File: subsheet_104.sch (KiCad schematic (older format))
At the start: 8 parts, among them U104 LM555_TIMER_PHY

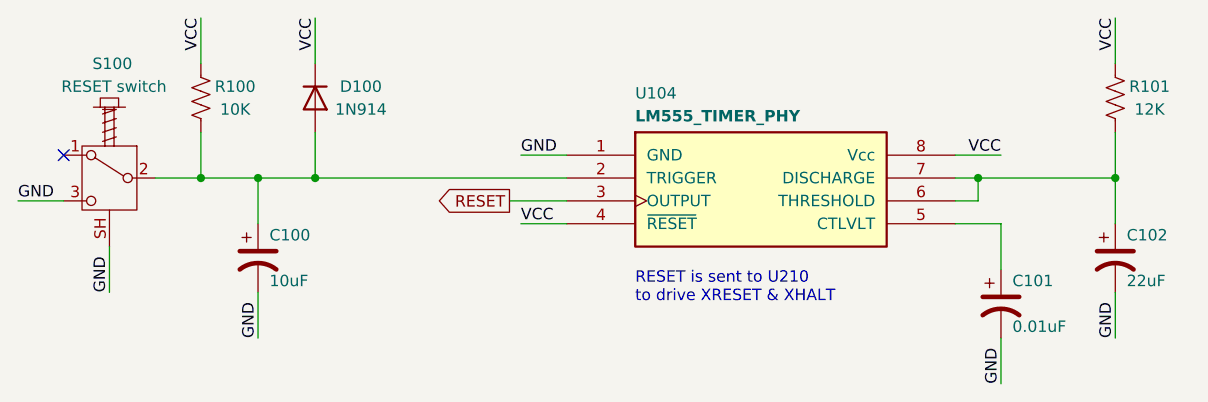
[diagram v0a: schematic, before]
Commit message: Resolves #6 : Apply the reset fix
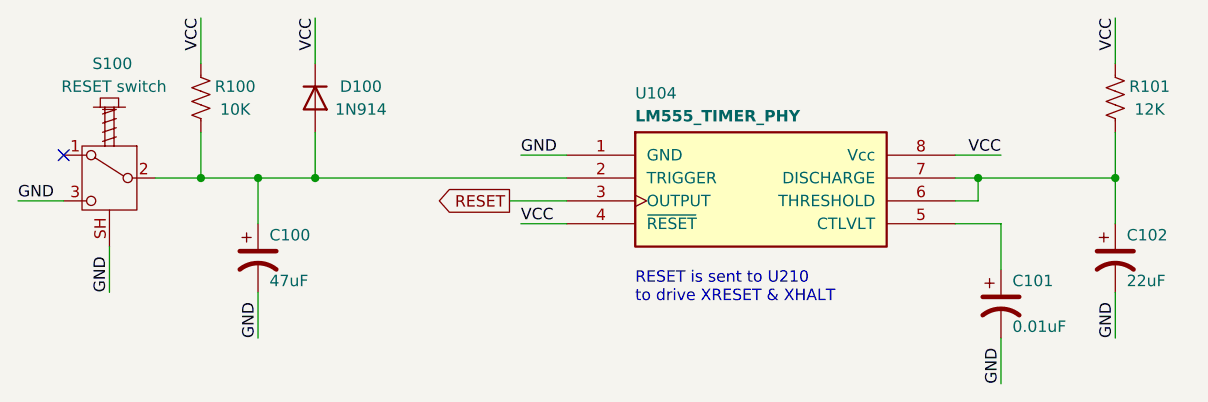
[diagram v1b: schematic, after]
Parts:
- C100: value 10uF -> 47uF
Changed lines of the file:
@@
 P 2750 2050
 F 0 "C100" H 2800 2150 50  0000 L CNN
-F 1 "10uF" H 2800 1950 50  0000 L CNN
+F 1 "47uF" H 2800 1950 50  0000 L CNN
 F 2 "commons_passives_THT:Passive_THT_capacitor_polarized_W5.08mm_L17.78mm" H 2750 2050 50  0001 C CNN
 F 3 "~" H 2750 2050 50  0001 C CNN

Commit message: Resolves #12 : Use the reference 'CP?' for polarized capacitors
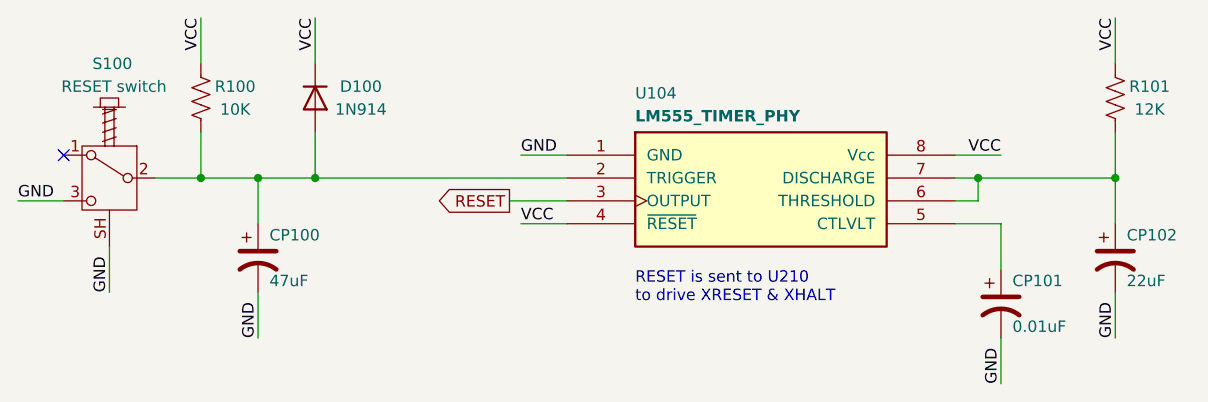
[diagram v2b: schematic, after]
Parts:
- renumbered C100 to CP100, C101 to CP101, C102 to CP102
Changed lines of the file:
@@
 VCC
 $Comp
-L Device:CP1 C100
+L Device:CP1 CP100
 U 1 1 608C1A6C
 P 2750 2050
-F 0 "C100" H 2800 2150 50  0000 L CNN
+F 0 "CP100" H 2800 2150 50  0000 L CNN
 F 1 "47uF" H 2800 1950 50  0000 L CNN
 F 2 "commons_passives_THT:Passive_THT_capacitor_polarized_W5.08mm_L17.78mm" H 2750 2050 50  0001 C CNN
@@
 	2750 2200 2750 2400
 $Comp
-L Device:CP1 C101
+L Device:CP1 CP101
 U 1 1 608C7F71
 P 6000 2250
-F 0 "C101" H 6050 2350 50  0000 L CNN
+F 0 "CP101" H 6050 2350 50  0000 L CNN
 F 1 "0.01uF" H 6050 2150 50  0000 L CNN
 F 2 "commons_passives_THT:Passive_THT_capacitor_W2.54mm_L10.16mm" H 6000 2250 50  0001 C CNN
@@
 	6000 2400 6000 2600
 $Comp
-L Device:CP1 C102
+L Device:CP1 CP102
 U 1 1 608C88D5
 P 6500 2050
-F 0 "C102" H 6550 2150 50  0000 L CNN
+F 0 "CP102" H 6550 2150 50  0000 L CNN
 F 1 "22uF" H 6550 1950 50  0000 L CNN
 F 2 "commons_passives_THT:Passive_THT_capacitor_polarized_W6.35mm_L20.32mm" H 6500 2050 50  0001 C CNN

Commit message: Resolves #13 : assign 1206 hand-solder footprints to resistors
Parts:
- R100, R101: footprint commons_passives_THT:Passive_THT_resistor_W2.54mm_L12.70mm -> Resistor_SMD:R_1206_3216Metric_Pad1.30x1.75mm_HandSolder
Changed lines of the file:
@@
 F 0 "R100" H 2650 1400 50  0000 C CNN
 F 1 "10K" H 2650 1300 50  0000 C CNN
-F 2 "commons_passives_THT:Passive_THT_resistor_W2.54mm_L12.70mm" V 2540 1340 50  0001 C CNN
+F 2 "Resistor_SMD:R_1206_3216Metric_Pad1.30x1.75mm_HandSolder" V 2540 1340 50  0001 C CNN
 F 3 "~" H 2500 1350 50  0001 C CNN
 	1    2500 1350
@@
 F 0 "R101" H 6650 1400 50  0000 C CNN
 F 1 "12K" H 6650 1300 50  0000 C CNN
-F 2 "commons_passives_THT:Passive_THT_resistor_W2.54mm_L12.70mm" V 6540 1340 50  0001 C CNN
+F 2 "Resistor_SMD:R_1206_3216Metric_Pad1.30x1.75mm_HandSolder" V 6540 1340 50  0001 C CNN
 F 3 "~" H 6500 1350 50  0001 C CNN
 	1    6500 1350

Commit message: Resolves #20 : Replace polarized capacitors CP101 and CP536 by unpolarized ones
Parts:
- C101: renamed from CP101; footprint commons_passives_THT:Passive_THT_capacitor_W2.54mm_L10.16mm -> Capacitor_SMD:C_1206_3216Metric_Pad1.33x1.80mm_HandSolder; symbol Device:CP1 -> Device:C_Small
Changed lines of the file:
@@
 	2750 2200 2750 2400
 $Comp
-L Device:CP1 CP101
+L Device:C_Small C101
 U 1 1 608C7F71
 P 6000 2250
-F 0 "CP101" H 6050 2350 50  0000 L CNN
+F 0 "C101" H 6050 2350 50  0000 L CNN
 F 1 "0.01uF" H 6050 2150 50  0000 L CNN
-F 2 "commons_passives_THT:Passive_THT_capacitor_W2.54mm_L10.16mm" H 6000 2250 50  0001 C CNN
+F 2 "Capacitor_SMD:C_1206_3216Metric_Pad1.33x1.80mm_HandSolder" H 6000 2250 50  0001 C CNN
 F 3 "~" H 6000 2250 50  0001 C CNN
 	1    6000 2250
@@
 Text Label 6000 2600 1    50   ~ 0
 GND
-Wire Wire Line
-	6000 1900 6000 2100
-Wire Wire Line
-	6000 2400 6000 2600
 $Comp
 L Device:CP1 CP102
@@
 Wire Wire Line
 	2100 2000 2100 2200
+Wire Wire Line
+	6000 1900 6000 2150
+Wire Wire Line
+	6000 2350 6000 2600
 $EndSCHEMATC

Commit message: Resolves #9 : Assign radial THT footprints to polarized capacitors
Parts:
- CP100: footprint commons_passives_THT:Passive_THT_capacitor_polarized_W5.08mm_L17.78mm -> Capacitor_THT:C_Radial_D6.3mm_H11.0mm_P2.50mm
- CP102: footprint commons_passives_THT:Passive_THT_capacitor_polarized_W6.35mm_L20.32mm -> Capacitor_THT:C_Radial_D5.0mm_H11.0mm_P2.00mm
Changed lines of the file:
@@
 F 0 "CP100" H 2800 2150 50  0000 L CNN
 F 1 "47uF" H 2800 1950 50  0000 L CNN
-F 2 "commons_passives_THT:Passive_THT_capacitor_polarized_W5.08mm_L17.78mm" H 2750 2050 50  0001 C CNN
+F 2 "Capacitor_THT:C_Radial_D6.3mm_H11.0mm_P2.50mm" H 2750 2050 50  0001 C CNN
 F 3 "~" H 2750 2050 50  0001 C CNN
 	1    2750 2050
@@
 F 0 "CP102" H 6550 2150 50  0000 L CNN
 F 1 "22uF" H 6550 1950 50  0000 L CNN
-F 2 "commons_passives_THT:Passive_THT_capacitor_polarized_W6.35mm_L20.32mm" H 6500 2050 50  0001 C CNN
+F 2 "Capacitor_THT:C_Radial_D5.0mm_H11.0mm_P2.00mm" H 6500 2050 50  0001 C CNN
 F 3 "~" H 6500 2050 50  0001 C CNN
 	1    6500 2050

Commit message: Resolves #16 : assign smd footprints to diodes
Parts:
- D100: footprint commons_passives_THT:Passive_THT_diode_W2.54mm_L12.70mm -> Diode_SMD:D_SOD-123F
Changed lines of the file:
@@
 F 0 "D100" V 2950 1550 50  0000 C CNN
 F 1 "1N914" V 3050 1550 50  0000 C CNN
-F 2 "commons_passives_THT:Passive_THT_diode_W2.54mm_L12.70mm" H 3000 1350 50  0001 C CNN
+F 2 "Diode_SMD:D_SOD-123F" H 3000 1350 50  0001 C CNN
 F 3 "~" H 3000 1350 50  0001 C CNN
 	1    3000 1350
